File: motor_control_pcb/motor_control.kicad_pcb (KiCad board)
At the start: 2 copper layers, 37 parts, among them J1 RND_Terminal_2P, J2 CONN_02X05, J3 RND_Terminal_3P, J4 RND_Terminal_3P, J5 RND_Terminal_3P, J6 RND_Terminal_2P, J7 RND_Terminal_2P, U0 MAX1000, U1 SN74LV1T126, U10 SN74LV1T126, U11 SN74LV1T126, U12 SN74LV1T126, U13 SN74LV1T126, U14 TSR_1-2433, U15 SN74LV1T126, U16 SN74LV1T126, U17 SN74LV1T126, U18 SN74LV1T126, U2 SN74LV1T126, U3 SN74LV1T126, U4 SN74LV1T126, U5 SN74LV1T126, U6 SN74LV1T126, U7 SN74LV1T126, U8 SN74LV1T126, U9 SN74LV1T126

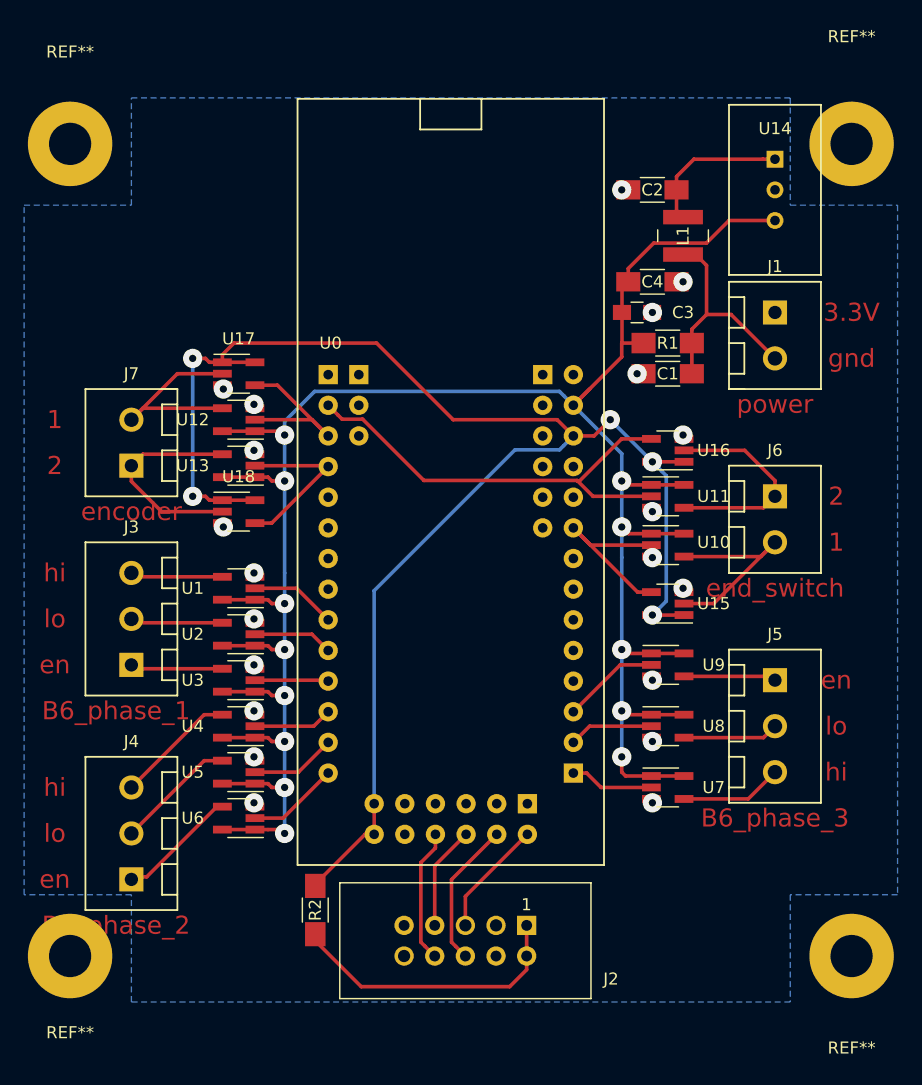
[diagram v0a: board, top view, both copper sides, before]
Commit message: vias korrigiert
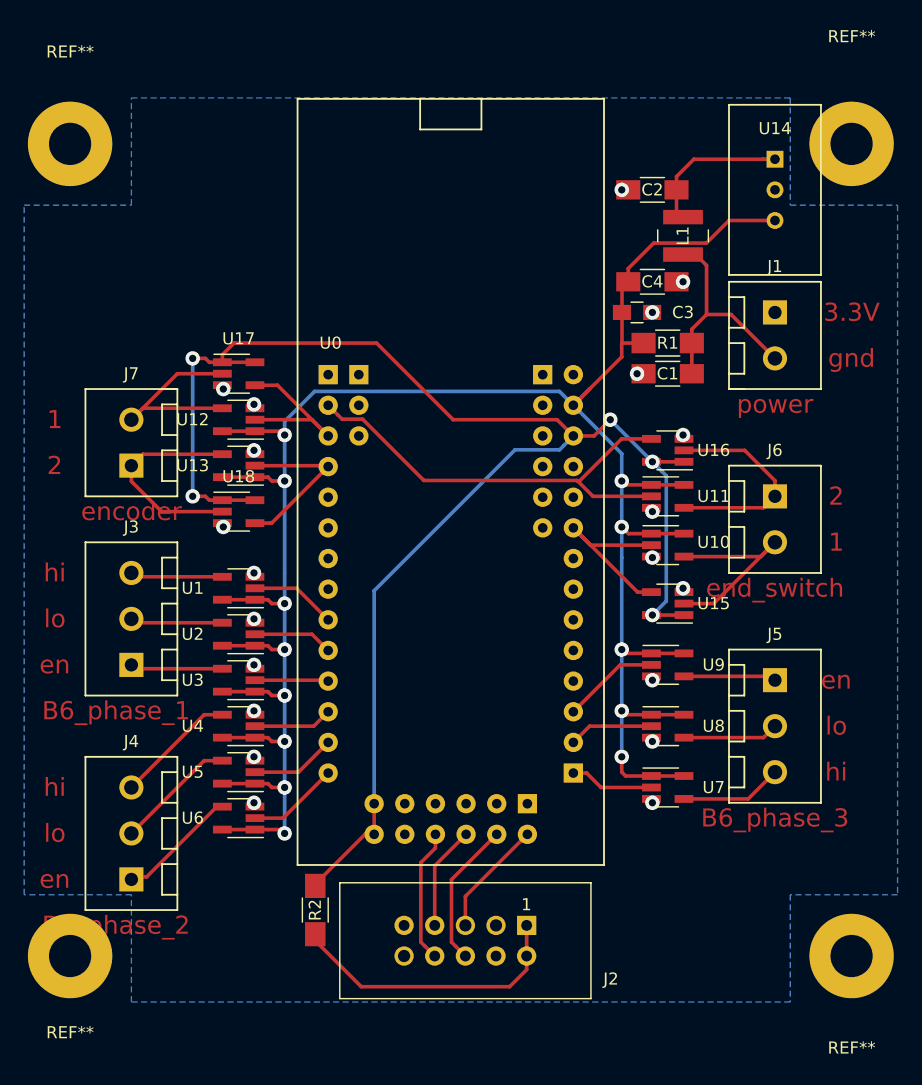
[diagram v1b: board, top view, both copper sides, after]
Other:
- net class Default: via_dia 1.6 -> 1.2
- rule via_min_size: 1.6 -> 1.2

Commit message: moved connectors
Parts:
- moved U14 47.0 mm to (102.9, 45.7)
- moved J3 6.35 mm to (96.5, 72.4)
- moved J4 6.35 mm to (96.5, 90.2)
- moved J7 6.35 mm to (96.5, 55.9)
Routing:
- net Net-(C2-Pad1): track 12.3 -> 43.2 mm
- net +5V: track 191.3 -> 212.8 mm
- net encoder_2_5: track 17.8 -> 21.7 mm
- net B6_1_low_5: track 7.67 -> 10.3 mm
- net B6_1_high_5: track 7.67 -> 10.3 mm
- net B6_1_enable_5: track 7.67 -> 10.3 mm
- net B6_2_enable_5: track 10.0 -> 7.67 mm
- net B6_2_low_5: track 10.0 -> 7.67 mm
- net B6_2_high_5: track 10.0 -> 7.67 mm
- net encoder_1_5: track 17.1 -> 14.8 mm
